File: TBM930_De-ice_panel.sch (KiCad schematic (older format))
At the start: 83 parts, among them J1 SW_AIRFRAME_DE_ICE, J10 AVR-ISP-6, J11 Screw_Terminal_01x02, J2 SW_ICE_LIGHT, J3 SW_PROP_DE_ICE, J4 SW_WIND_SHIELD, J5 SW_PITOT_L_HTR, J6 SW_PITOT_R_HTR, J7 SW_INERT_SEP, J8 Barrel_Jack, J9 USB_B_Mini, SW1 SW_Push, SW2 SW_Push, U1 TLC5917IN, U2 TLC5917IN, U3 ATmega32U4-MU, Y1 Crystal_GND24

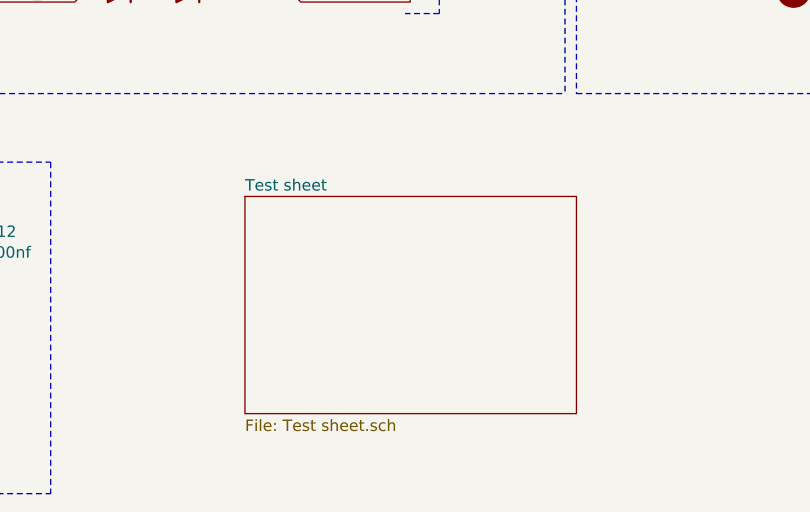
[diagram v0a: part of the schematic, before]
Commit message: Rename subsheet
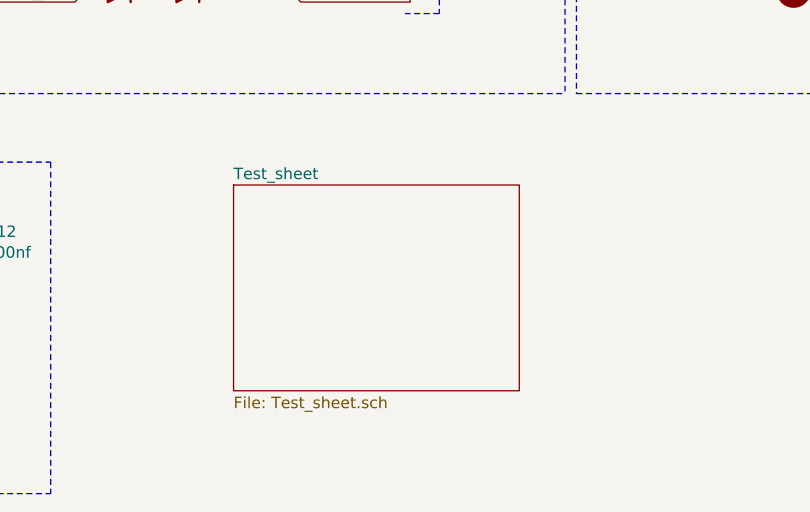
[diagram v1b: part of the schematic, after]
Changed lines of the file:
@@
 	8850 4050 8850 3450
 $Sheet
-S 7400 6250 1450 950
-U 614A4178
-F0 "Test sheet" 50
-F1 "Test sheet.sch" 50
+S 7350 6200 1250 900
+U 614A4370
+F0 "Test_sheet" 50
+F1 "Test_sheet.sch" 50
 $EndSheet
 $EndSCHEMATC
